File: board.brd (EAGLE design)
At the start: 50 x 50 mm, 11 parts

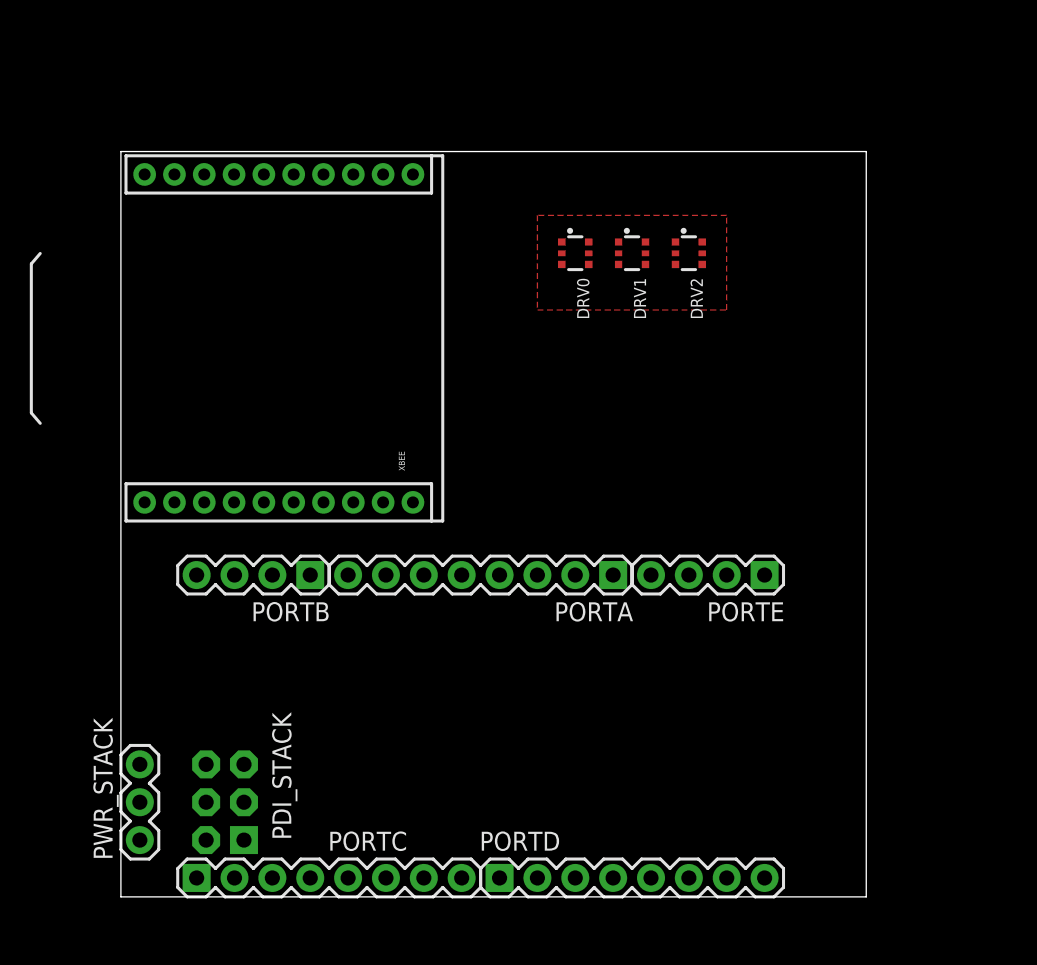
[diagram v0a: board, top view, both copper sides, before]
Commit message: add general ground pours
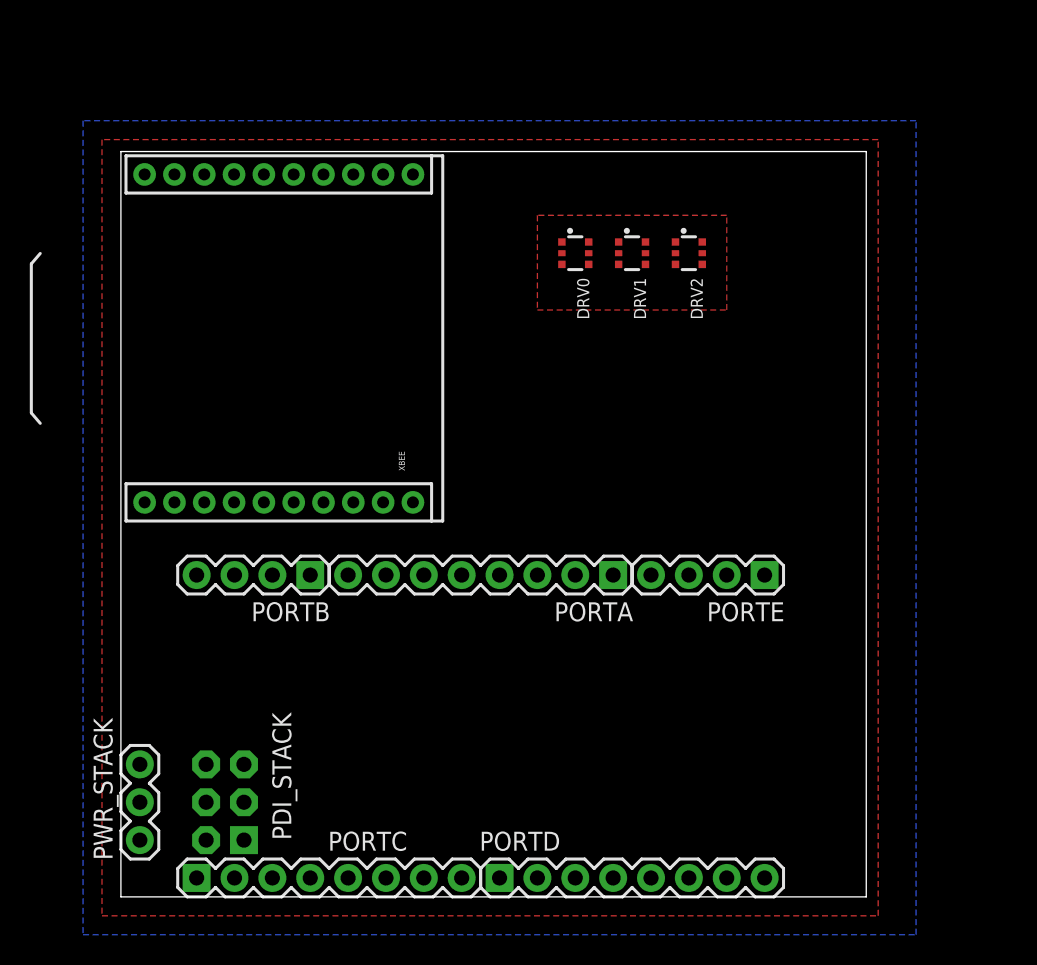
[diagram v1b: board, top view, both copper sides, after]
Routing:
- added copper zone on layer 1, net GND
- added copper zone on layer 16, net GND
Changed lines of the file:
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@@
 <contactref element="PDI_STACK" pad="6"/>
 <contactref element="PWR_STACK" pad="2"/>
-<wire x1="40.64" y1="1.27" x2="43.18" y2="1.27" width="0" layer="19" extent="1-1"/>
-<wire x1="19.59" y1="26.465" x2="40.64" y2="1.27" width="0" layer="19" extent="1-1"/>
-<wire x1="5.715" y1="8.89" x2="19.59" y2="26.465" width="0" layer="19" extent="1-1"/>
-<wire x1="1.27" y1="6.35" x2="5.715" y2="8.89" width="0" layer="19" extent="1-1"/>
+<polygon width="0.4064" layer="1" isolate="0.254" rank="6">
+<vertex x="-1.27" y="50.8"/>
+<vertex x="-1.27" y="-1.27"/>
+<vertex x="50.8" y="-1.27"/>
+<vertex x="50.8" y="50.8"/>
+</polygon>
+<polygon width="0.4064" layer="16" isolate="0.254" rank="6">
+<vertex x="-2.54" y="52.07"/>
+<vertex x="-2.54" y="-2.54"/>
+<vertex x="53.34" y="-2.54"/>
+<vertex x="53.34" y="52.07"/>
+</polygon>
 </signal>
 <signal name="VDD">
@@
 <contactref element="DRV2" pad="1"/>
 <contactref element="DRV1" pad="1"/>
-<polygon width="0.4064" layer="1" isolate="0.254" rank="6">
+<polygon width="0.4064" layer="1" isolate="0.254" rank="5">
 <vertex x="27.94" y="45.72"/>
 <vertex x="27.94" y="39.37"/>

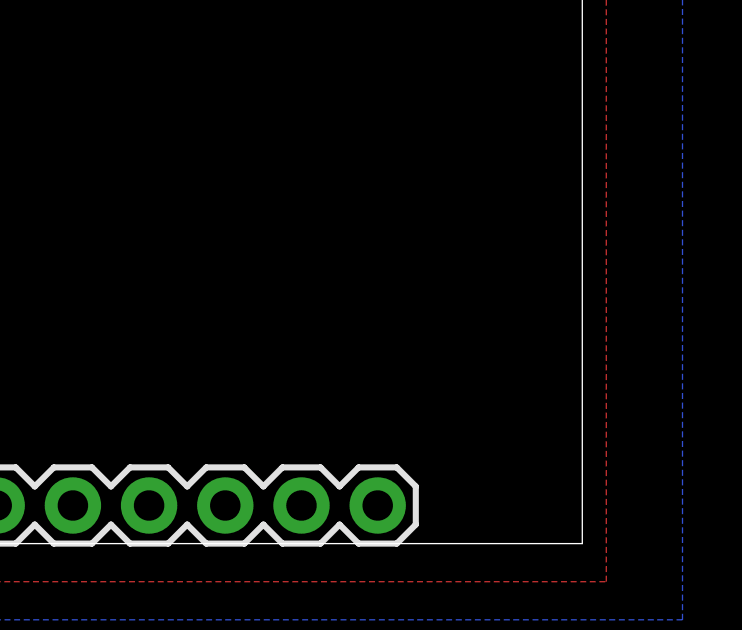
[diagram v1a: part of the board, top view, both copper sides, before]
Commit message: added JST battery connector, alternatively 2.54mm pin header can be used
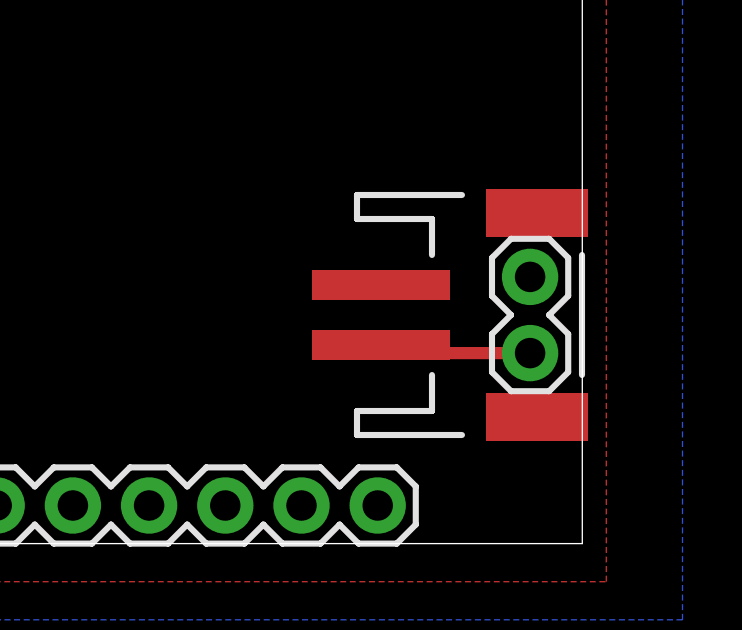
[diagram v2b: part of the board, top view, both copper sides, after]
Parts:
- added BAT: (no value), SparkFun-Connectors:JST-2-SMD
- added BAT_ALT: (no value), SparkFun-Connectors:1X02
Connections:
- new net VBAT: BAT.2, BAT_ALT.2
- net GND: now also BAT.1, BAT_ALT.1
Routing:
- net VBAT: track 0.00 -> 5.24 mm
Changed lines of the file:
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@@
 <element name="DRV1" library="microbuilder" package="SOT363" value="" x="34.29" y="43.18" rot="R270"/>
 <element name="DRV2" library="microbuilder" package="SOT363" value="" x="38.1" y="43.18" rot="R270"/>
+<element name="BAT" library="SparkFun-Connectors" package="JST-2-SMD" value="" x="46.99" y="7.62" smashed="yes" rot="R270">
+<attribute name="PROD_ID" value="CONN-08352" x="46.99" y="7.62" size="1.778" layer="27" rot="R270" display="off"/>
+<attribute name="VALUE" x="46.99" y="8.89" size="0.4064" layer="27" rot="R270"/>
+</element>
+<element name="BAT_ALT" library="SparkFun-Connectors" package="1X02" value="" x="48.26" y="8.89" smashed="yes" rot="R270">
+<attribute name="VALUE" x="45.085" y="10.16" size="1.27" layer="27" rot="R270"/>
+</element>
 </elements>
 <signals>
@@
 <vertex x="53.34" y="52.07"/>
 </polygon>
+<contactref element="BAT" pad="1"/>
+<contactref element="BAT_ALT" pad="1"/>
 </signal>
 <signal name="VDD">
@@
 <wire x1="17.78" y1="1.27" x2="39" y2="43.18" width="0" layer="19" extent="1-1"/>
 </signal>
+<signal name="VBAT" class="1">
+<contactref element="BAT" pad="2"/>
+<contactref element="BAT_ALT" pad="2"/>
+<wire x1="48.26" y1="6.35" x2="43.29" y2="6.35" width="0.4064" layer="1"/>
+<wire x1="43.29" y1="6.35" x2="43.29" y2="6.62" width="0.4064" layer="1"/>
+</signal>
 </signals>

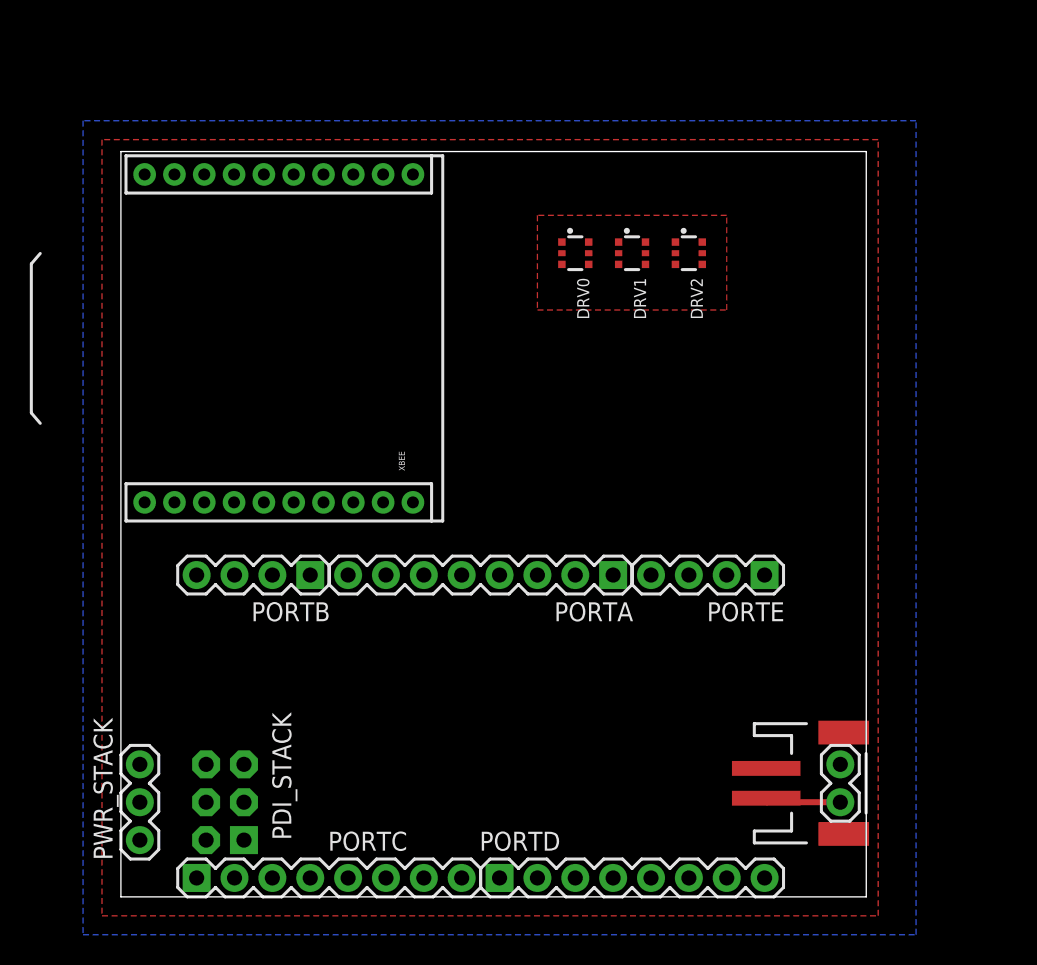
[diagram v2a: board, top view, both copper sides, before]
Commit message: placed the led drivers and connectors
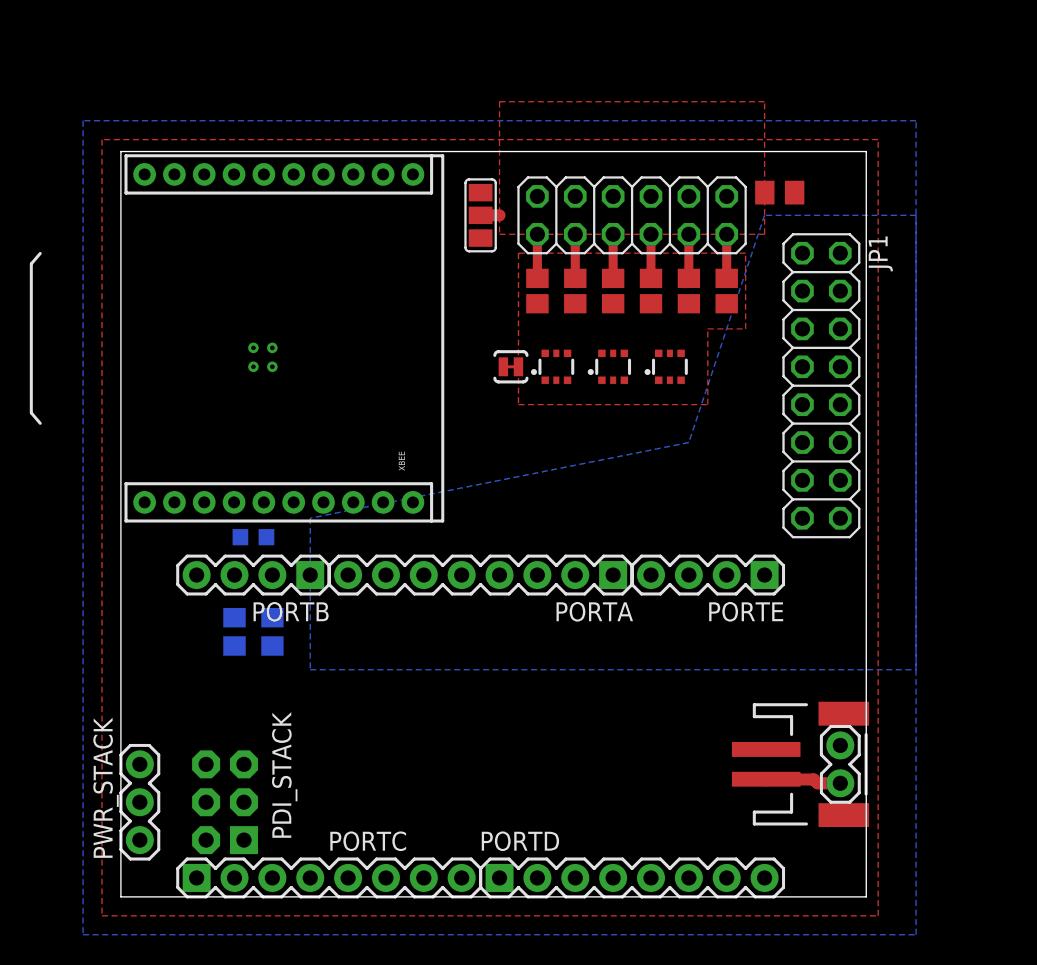
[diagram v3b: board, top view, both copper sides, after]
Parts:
- added C1: 0.1uF, rcl:C0603K
- added C2: (no value), resistor:C0805K
- added JP1: (no value), pinhead:2X08
- added JP2: (no value), pinhead:2X06
- added R1: 100k, rcl:R0805
- added R2: 50k, rcl:R0805
- added RLED0, RLED1, RLED2, RLED3, RLED4, RLED5: (no value), resistor:R0805
- added SJ1: SOLDERJUMPERTRACE, SparkFun-Passives:SJ_2S-TRACE
- added SJ2: (no value), SparkFun-Passives:SJ_2
- moved DRV2 7.73 mm to (36.8, 35.6), turned to 0 degrees
- moved DRV0 7.73 mm to (29.2, 35.6), turned to 0 degrees
- moved DRV1 7.73 mm to (33.0, 35.6), turned to 0 degrees
- moved BAT 1.27 mm to (47.0, 8.89)
- moved BAT_ALT 1.27 mm to (48.3, 10.2)
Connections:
- removed net VDD: XBEE.1
- new net +3V3: SJ2.3, XBEE.1
- new net AGND: JP1.10, JP1.12, JP1.14, JP1.16, JP1.2, JP1.4, JP1.6, JP1.8
- new net LED0: DRV0.6, RLED0.1
- new net LED0R: JP2.1, RLED0.2
- new net LED1: DRV0.3, RLED1.1
- new net LED1R: JP2.3, RLED1.2
- new net LED2: DRV1.6, RLED2.1
- new net LED2R: JP2.5, RLED2.2
- new net LED3: DRV1.3, RLED3.1
- new net LED3R: JP2.7, RLED3.2
- new net LED4: DRV2.6, RLED4.1
- new net LED4R: JP2.9, RLED4.2
- new net LED5: DRV2.3, RLED5.1
- new net LED5R: JP2.11, RLED5.2
- new net PA0: JP1.15, PORTA.1
- new net PA1: JP1.13, PORTA.2
- new net PA2: JP1.11, PORTA.3
- new net PA3: JP1.9, PORTA.4
- new net PA4: JP1.7, PORTA.5
- new net PA5: JP1.5, PORTA.6
- new net PA6: JP1.3, PORTA.7
- new net PA7: JP1.1, PORTA.8
- new net VBAT_SENSE: C1.1, PORTB.2, R1.1, R2.2
- new net VLED: C2.1, JP2.10, JP2.12, JP2.2, JP2.4, JP2.6, JP2.8, SJ2.2
- net GND: now also C1.2, C2.2, R2.1, SJ1.1
- net GND_PWR: now also SJ1.2
- net VBAT: now also R1.2, SJ2.1
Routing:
- net LED5R: track 0.00 -> 2.96 mm
- net LED4R: track 0.00 -> 2.96 mm
- net LED3R: track 0.00 -> 2.96 mm
- net LED2R: track 0.00 -> 2.96 mm
- net LED1R: track 0.00 -> 2.96 mm
- net LED0R: track 0.00 -> 2.96 mm
- net VLED: track 0.00 -> 1.27 mm
- added copper zone on layer 16, net AGND
- added copper zone on layer 1, net VLED
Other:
- board text added: "Battery sense (optional)"

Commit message: this header must be 90deg one, otherwise it will not fit under the xbee
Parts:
- removed JP2: (no value), pinhead:2X06
- added JP3: (no value), pinhead:2X06/90
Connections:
- net LED0R: now also JP3.1; no longer JP2.1
- net LED1R: now also JP3.3; no longer JP2.3
- net LED2R: now also JP3.5; no longer JP2.5
- net LED3R: now also JP3.7; no longer JP2.7
- net LED4R: now also JP3.9; no longer JP2.9
- net LED5R: now also JP3.11; no longer JP2.11
- net VLED: now also JP3.10, JP3.12, JP3.2, JP3.4, JP3.6, JP3.8; no longer JP2.10, JP2.12, JP2.2, JP2.4, JP2.6, JP2.8
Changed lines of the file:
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@@
 <element name="C1" library="rcl" package="C0603K" value="0.1uF" x="8.89" y="24.13" smashed="yes" rot="MR0"/>
 <element name="JP1" library="pinhead" package="2X08" value="" x="46.99" y="34.29" rot="R270"/>
-<element name="JP2" library="pinhead" package="2X06" value="" x="34.29" y="45.72" smashed="yes">
-<attribute name="VALUE" x="26.67" y="41.275" size="1.27" layer="27"/>
-</element>
 <element name="SJ2" library="SparkFun-Passives" package="SJ_2" value="" x="24.13" y="45.72" smashed="yes" rot="R270">
 <attribute name="VALUE" x="24.13" y="45.8201" size="0.02" layer="27" rot="R270"/>
@@
 </element>
 <element name="SJ1" library="SparkFun-Passives" package="SJ_2S-TRACE" value="SOLDERJUMPERTRACE" x="26.162" y="35.56" smashed="yes"/>
+<element name="JP3" library="pinhead" package="2X06/90" value="" x="34.29" y="50.8"/>
 </elements>
 <signals>
@@
 </signal>
 <signal name="VLED">
-<contactref element="JP2" pad="12"/>
-<contactref element="JP2" pad="2"/>
-<contactref element="JP2" pad="10"/>
-<contactref element="JP2" pad="8"/>
-<contactref element="JP2" pad="6"/>
-<contactref element="JP2" pad="4"/>
 <polygon width="0.4064" layer="1" isolate="0.254" rank="5">
 <vertex x="25.4" y="53.34"/>
@@
 <wire x1="24.13" y1="45.72" x2="25.4" y2="45.72" width="0.8128" layer="1"/>
 <contactref element="C2" pad="1"/>
+<contactref element="JP3" pad="2"/>
+<contactref element="JP3" pad="4"/>
+<contactref element="JP3" pad="6"/>
+<contactref element="JP3" pad="8"/>
+<contactref element="JP3" pad="10"/>
+<contactref element="JP3" pad="12"/>
 </signal>
 <signal name="LED1" class="1">
@@
 </signal>
 <signal name="LED0R" class="1">
-<contactref element="JP2" pad="1"/>
 <contactref element="RLED0" pad="2"/>
+<contactref element="JP3" pad="1"/>
 <wire x1="27.94" y1="41.49" x2="27.94" y2="44.45" width="0.6096" layer="1"/>
 </signal>
 <signal name="LED1R" class="1">
-<contactref element="JP2" pad="3"/>
 <contactref element="RLED1" pad="2"/>
+<contactref element="JP3" pad="3"/>
 <wire x1="30.48" y1="41.49" x2="30.48" y2="44.45" width="0.6096" layer="1"/>
 </signal>
 <signal name="LED2R" class="1">
-<contactref element="JP2" pad="5"/>
 <contactref element="RLED2" pad="2"/>
+<contactref element="JP3" pad="5"/>
 <wire x1="33.02" y1="41.49" x2="33.02" y2="44.45" width="0.6096" layer="1"/>
 </signal>
 <signal name="LED3R" class="1">
-<contactref element="JP2" pad="7"/>
 <contactref element="RLED3" pad="2"/>
+<contactref element="JP3" pad="7"/>
 <wire x1="35.56" y1="41.49" x2="35.56" y2="44.45" width="0.6096" layer="1"/>
 </signal>
 <signal name="LED4R" class="1">
-<contactref element="JP2" pad="9"/>
 <contactref element="RLED4" pad="2"/>
+<contactref element="JP3" pad="9"/>
 <wire x1="38.1" y1="41.49" x2="38.1" y2="44.45" width="0.6096" layer="1"/>
 </signal>
 <signal name="LED5R" class="1">
-<contactref element="JP2" pad="11"/>
 <contactref element="RLED5" pad="2"/>
+<contactref element="JP3" pad="11"/>
 <wire x1="40.64" y1="41.49" x2="40.64" y2="44.45" width="0.6096" layer="1"/>
 </signal>
